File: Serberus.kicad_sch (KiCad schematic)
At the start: 108 parts, among them J1 USB_C_Receptacle_USB2.0, J2 UART 1,3,4, J3 SWD/JTAG2, J4 LA, J5 SPI, J6 CORTEX, J7 I2C, J8 iCE40, J9 V_Merge, Q1 BSH103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

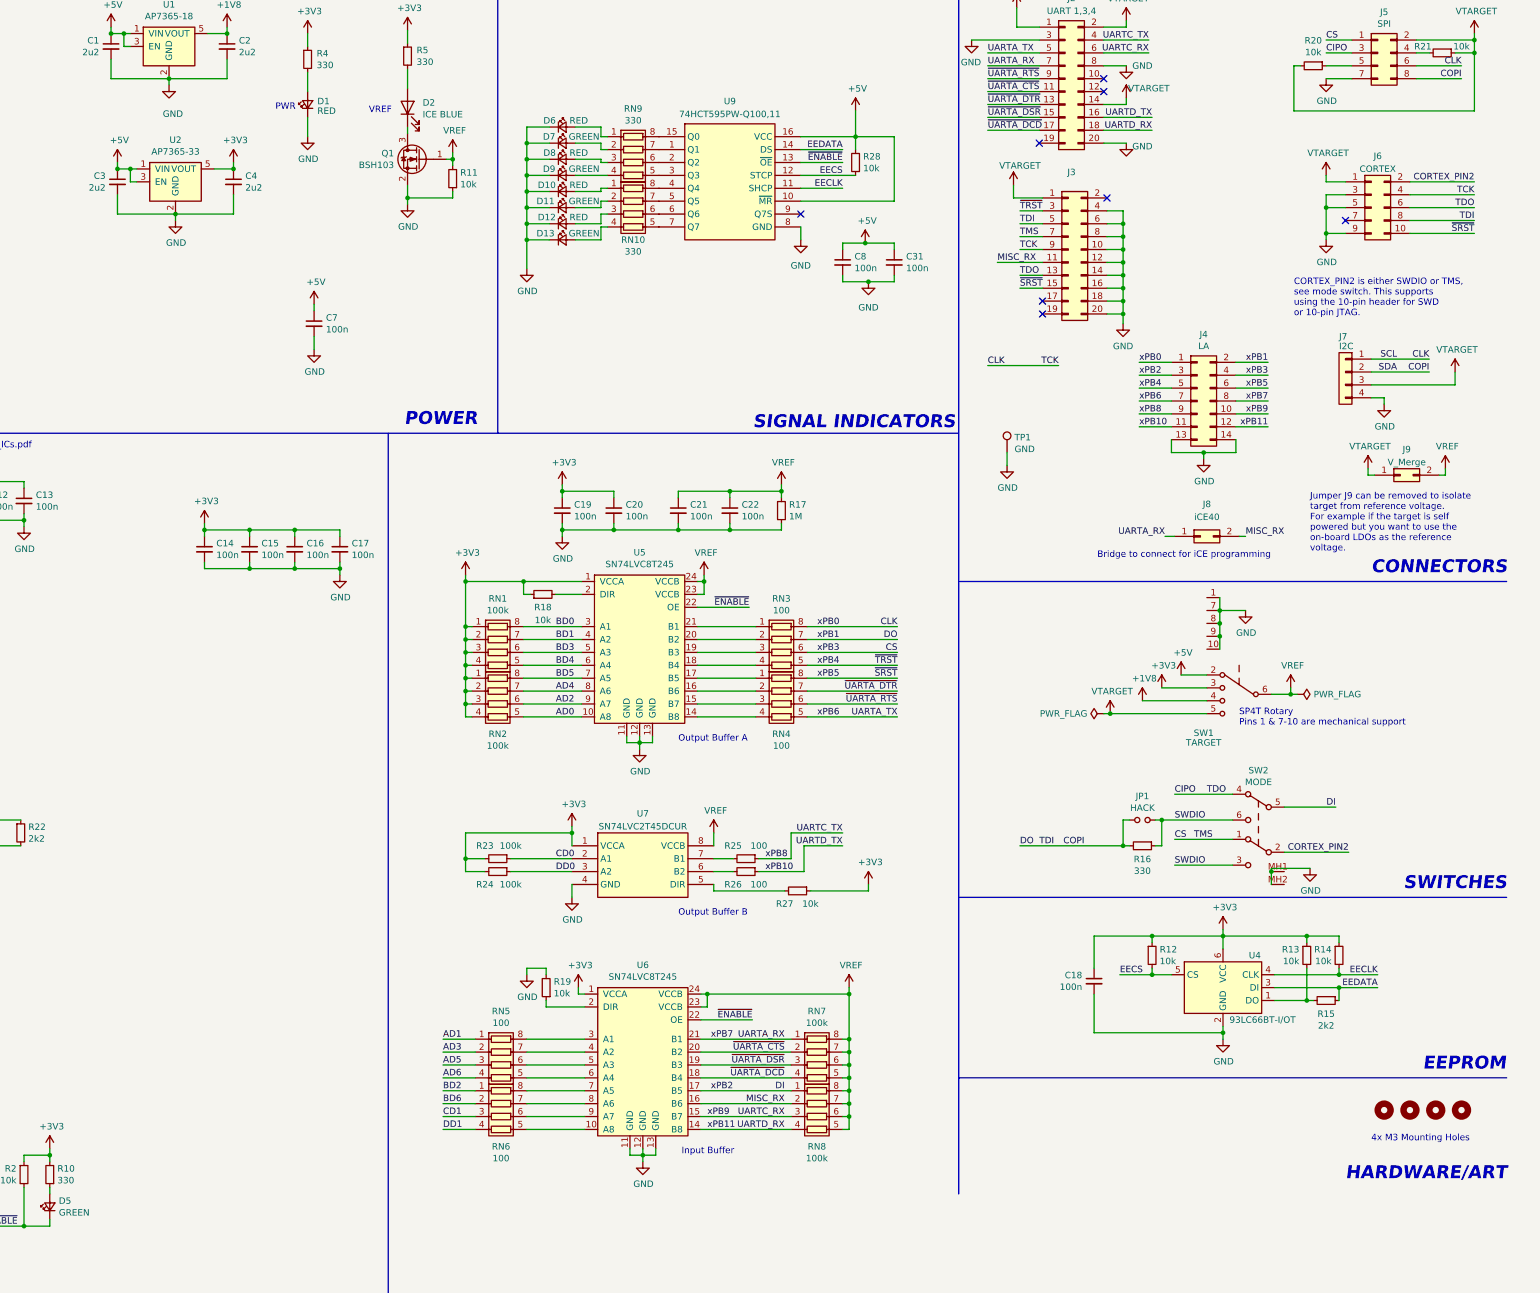
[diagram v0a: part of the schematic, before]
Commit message: Prototype Run 1
Cleaned up libraries for easy export/import. Reversed Polarity of J3, added labels and notes to silkscreen layer. Final version for first prototype run.
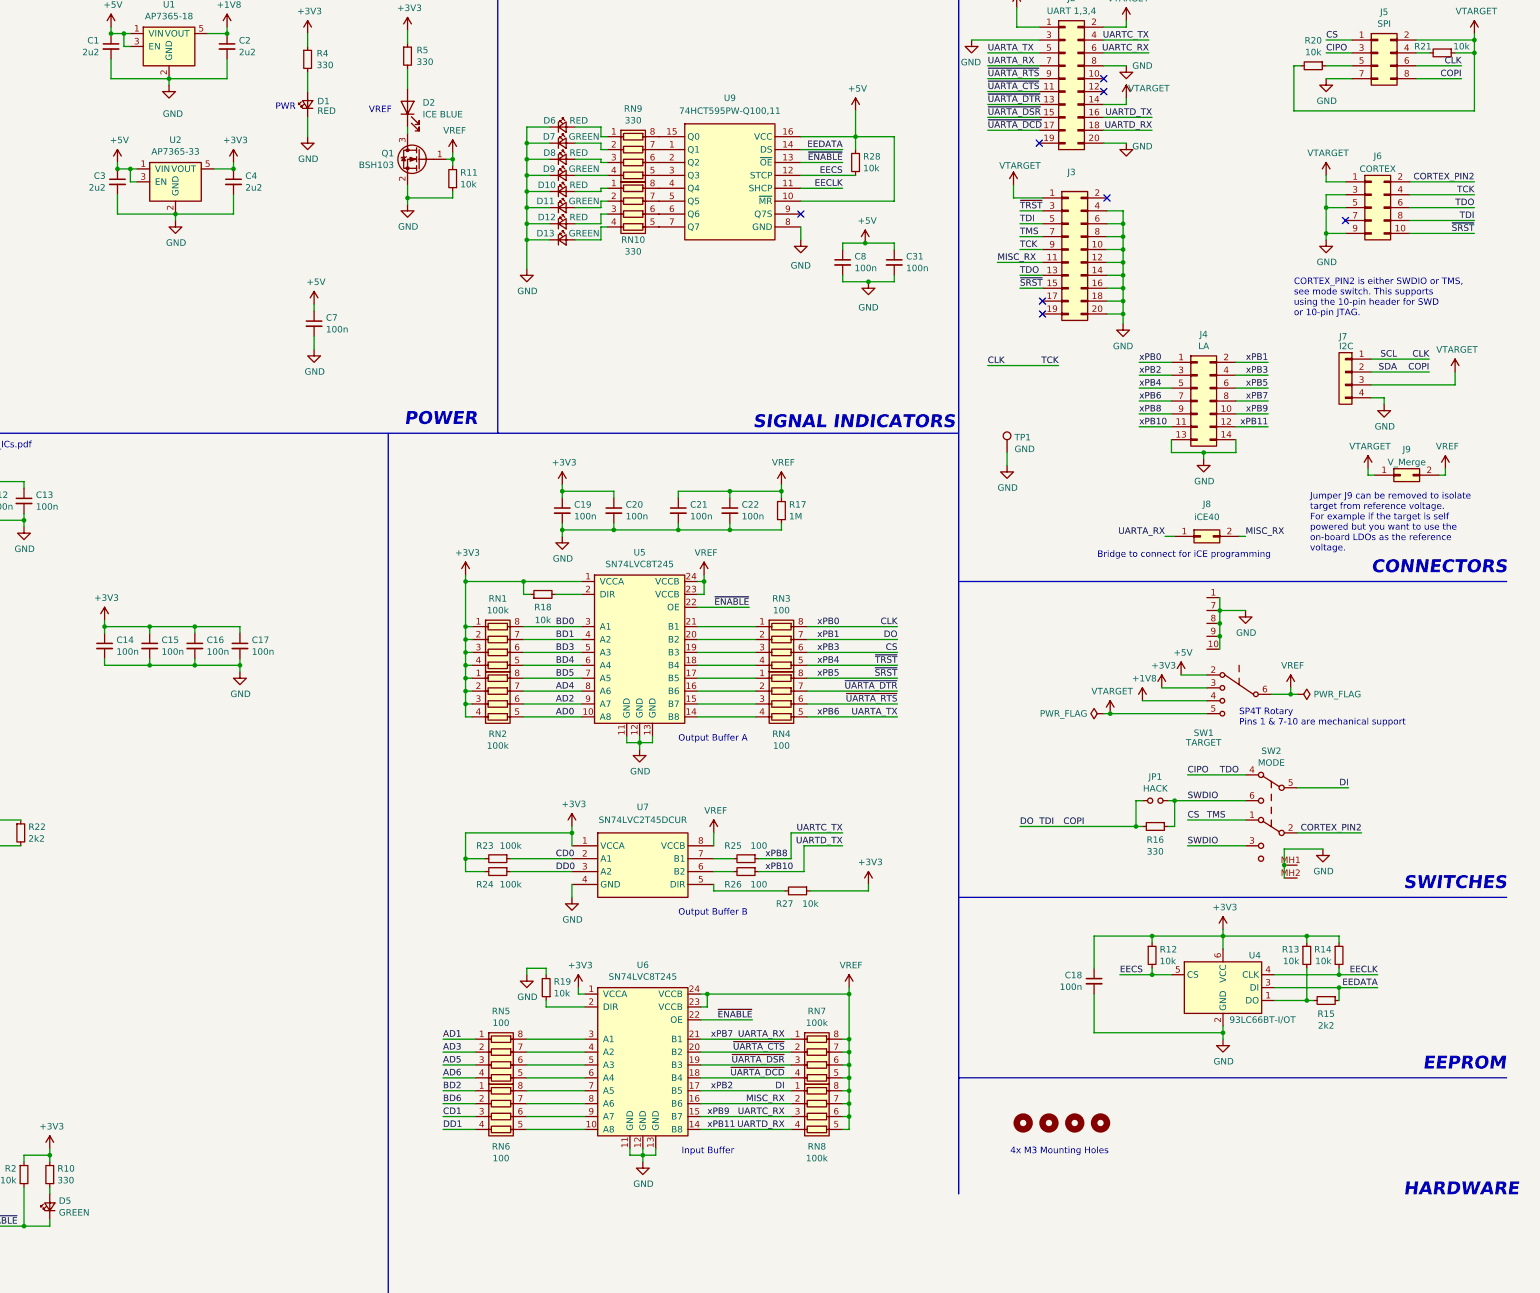
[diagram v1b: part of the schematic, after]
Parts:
- FB1, FB3: symbol Serberus-rescue:Ferrite_Bead_Small-Device -> Device:FerriteBead_Small
- JP1: symbol Serberus-rescue:Jumper_NO_Small-Device -> Serberus:Jumper_NO_Small-Device; now in the parts list
- R23, R24: Key res-0402-2k2 -> res-0402-100k; LCSC C25879 -> C25741; P/N 0402WGF2201TCE -> 0402WGF1003TCE
- R25: Key res-0402-2k2 -> res-0402-100; LCSC C25879 -> C25076; P/N 0402WGF2201TCE -> 0402WGF1000TCE
- R26: Key res-0402-2k2 -> res-0402-100
- RN10, RN9: Key res-0402cv-array-4-100 -> res-0402cv-array-4-330; LCSC C48442 -> C43557; P/N 4D02WGJ0101TCE -> 4D02WGJ0331TCE
- SW1: symbol GooSe-rescue:SW_DP4T-tigard -> Serberus:SW_DP4T-Rotary
- U3: symbol FT4233HPQ-TRAY:FT4233HPQ-TRAY -> Serberus:FT4233HPQ-TRAY
- U7: symbol 2Bit_Level_Shifter:SN74LVC2T45DCUR -> Serberus:SN74LVC2T45DCUR
- U8: symbol USB_C_PROT:DPO2036DBB-7 -> Serberus:DPO2036DBB-7
- U9: symbol Indicator_driver:74HCT595PW-Q100,11 -> Serberus:74HCT595PW-Q100,11
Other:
- note added: "HARDWARE"
- note removed: "HARDWARE/ART"
- moved on the sheet: C14, C15, C16, C17, JP1, R16

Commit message: Update Schematic
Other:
- note added: "CORTEX_PIN2 switches TMS and SWDIO via SW2."
- note removed: "CORTEX_PIN2 is either SWDIO or TMS, see mode switch. This supports using the 10-pin header for SWD or 10-pin JTAG."
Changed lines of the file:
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@@
     (effects (font (size 1.27 1.27)) (justify left bottom))
   )
-  (text "CORTEX_PIN2 is either SWDIO or TMS,\nsee mode switch. This supports\nusing the 10-pin header for SWD\nor 10-pin JTAG."
-    (at 365.76 78.74 0)
+  (text "CORTEX_PIN2 switches TMS and\nSWDIO via SW2. \n" (at 370.205 74.295 0)
     (effects (font (size 1.27 1.27)) (justify left bottom))
   )

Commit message: Update Serberus.kicad_sch
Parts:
- J4: P/N FTSH-107-01-F-DV-K -> 77313-103-14LF
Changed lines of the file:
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@@
     (effects (font (size 1.27 1.27)) (justify left bottom))
   )
-  (text "CORTEX_PIN2 switches TMS and\nSWDIO via SW2. \n" (at 370.205 74.295 0)
+  (text "CORTEX_PIN2 switches TMS and\nSWDIO via SW2. \n" (at 370.205 74.93 0)
     (effects (font (size 1.27 1.27)) (justify left bottom))
   )
@@
       (effects (font (size 1.27 1.27)) hide)
     )
-    (property "P/N" "FTSH-107-01-F-DV-K" (at 346.71 95.25 0)
-      (effects (font (size 1.27 1.27)) hide)
-    )
+    (property "P/N" "77313-103-14LF" (at 346.71 95.25 0)
+      (effects (font (size 1.27 1.27)) hide)
+    )

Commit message: Update Serberus.kicad_sch
Updated part numbers for rotary switch.
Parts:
- SW1: Manufacturer_Part_Number NR01105ANG13-2A -> NR01104ANG13-2A; Mouser Part Number 633-NR01105ANG13-2A -> 633-NR01104ANG13-2A
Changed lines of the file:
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@@
       (effects (font (size 1.27 1.27)) hide)
     )
-    (property "Manufacturer_Part_Number" "NR01105ANG13-2A" (at 362.585 144.145 0)
+    (property "Manufacturer_Part_Number" "NR01104ANG13-2A" (at 362.585 144.145 0)
       (effects (font (size 1.27 1.27)) hide)
     )
@@
       (effects (font (size 1.27 1.27)) hide)
     )
-    (property "Mouser Part Number" "633-NR01105ANG13-2A" (at 349.885 153.035 0)
+    (property "Mouser Part Number" "633-NR01104ANG13-2A" (at 349.885 153.035 0)
       (effects (font (size 2.54 2.54)) hide)
     )
